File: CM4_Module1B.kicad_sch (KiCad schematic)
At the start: 10 parts, among them J18 179-UJ20CHC4SMTTR

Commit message: chore: Many routing changes
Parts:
- removed J18: 179-UJ20CHC4SMTTR, dz_con:CON_Samesky_CUI_UJ20-C-H-C-4-SMT-TR, symbol #dzdb:s_con/SAME-179-UJ20CHC4SMTTR
- added J3: 179-UJ20CHC4SMTTR, dz_con:CON_Samesky_CUI_UJ20-C-H-C-4-SMT-TR, symbol #dzdb:s_con/SAME-179-UJ20CHC4SMTTR
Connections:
- net GND: now also J3.A12_B1 (GND), J3.A1_B12 (GND)
- net USB_D+: now also J3.A6 (DP1), J3.B6 (DP2)
- net USB_D-: now also J3.A7 (DN1), J3.B7 (DN2)
- net at C20.2, R11.1: now also J3.SH1 (SHIELD), J3.SH2 (SHIELD), J3.SH3 (SHIELD), J3.SH4 (SHIELD)
- net at R10.1: now also J3.A5 (CC1)
- net at R12.1: now also J3.B5 (CC2)
- net PCIe_CLK_N renamed PCIE_CLK._N
- net PCIe_CLK_P renamed PCIE_CLK._P
- net PCIe_RX_N renamed PCIE_RX._N
- net PCIe_RX_P renamed PCIE_RX._P
- net PCIe_TX_N renamed PCIE_TX._N
- net PCIe_TX_P renamed PCIE_TX._P
- net USB_Out_5V renamed USB_OTG_5V
- net USB_OTG_5V: now also J3.A4_B9 (VBUS), J3.A9_B4 (VBUS)
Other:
- note removed: "indicator LED :)"
- note removed: "reduce EMI"
- moved on the sheet: C20, D5, D6, R10, R11, R12, R9

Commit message: chore: more cleanup
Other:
- company: (none) -> Davide
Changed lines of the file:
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@@
 	(generator_version "9.0")
 	(paper "A4")
+	(title_block
+		(date "2025-11-18")
+		(company "Davide")
+	)
 	(text "old usb port for reference."
 		(exclude_from_sim no)

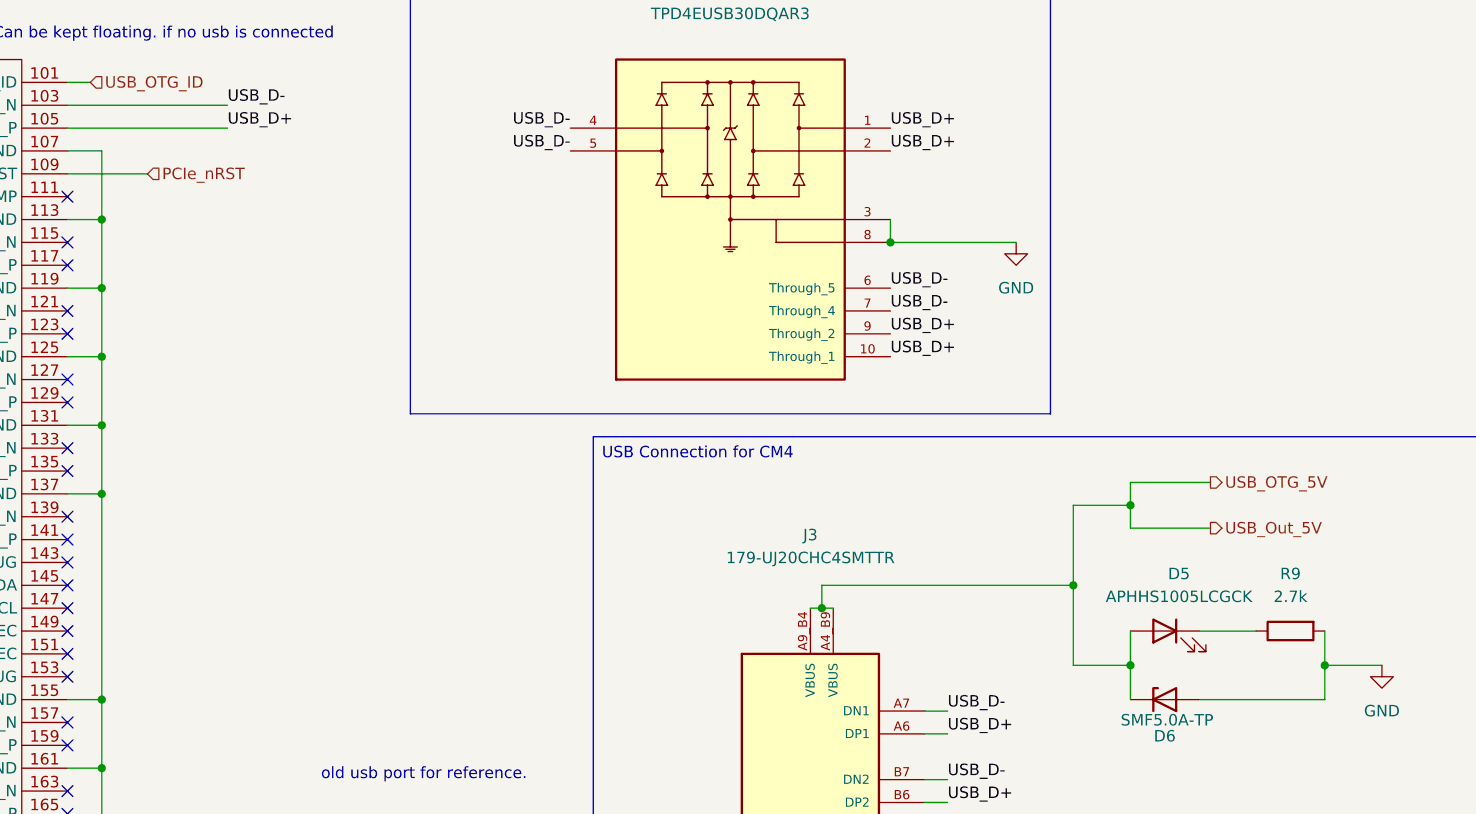
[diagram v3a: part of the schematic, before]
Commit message: chore: added LED indicators for power and activity status, updated symbold, rerouted some things for better visibility
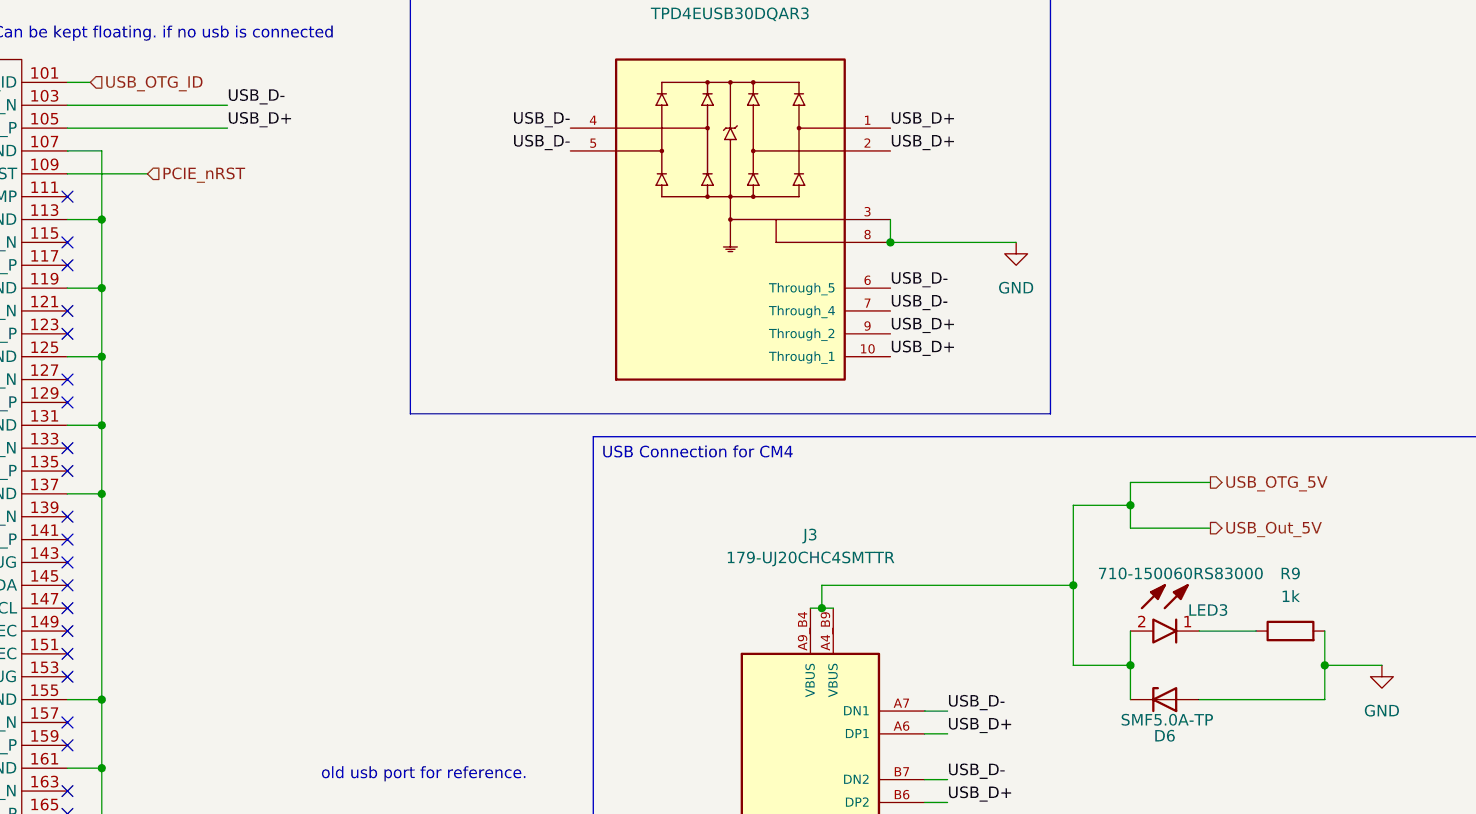
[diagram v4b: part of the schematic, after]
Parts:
- removed D5: APHHS1005LCGCK, LED_SMD:LED_0402_1005Metric, symbol #dzdb:s_dio/D-KIN-APHHS1005LCGCK
- removed R9: 2.7k, Resistor_SMD:R_0603_1608Metric, symbol #dzdb:g_res/R-2.7k-0603
- added LED3: 710-150060RS83000, dz_dio:Wuerth_LED_150060RS83000, symbol #dzdb:s_dio/D-WURT-710-150060RS83000
- added R9: 1k, Resistor_SMD:R_0603_1608Metric, symbol #dzdb:g_res/R-1k-0603
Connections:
- net GND: now also R9.2
- net USB_OTG_5V: now also LED3.2 (A)
- net PCIe_nRST renamed PCIE_nRST
- new net: LED3.1 (K), R9.1

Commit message: chore: Loads of redoing stuff. Added a Changelog
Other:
- title: (none) -> Nautilus_Mainboard
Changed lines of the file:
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@@
 	(paper "A4")
 	(title_block
+		(title "Nautilus_Mainboard")
 		(date "2025-11-19")
 		(rev "0")

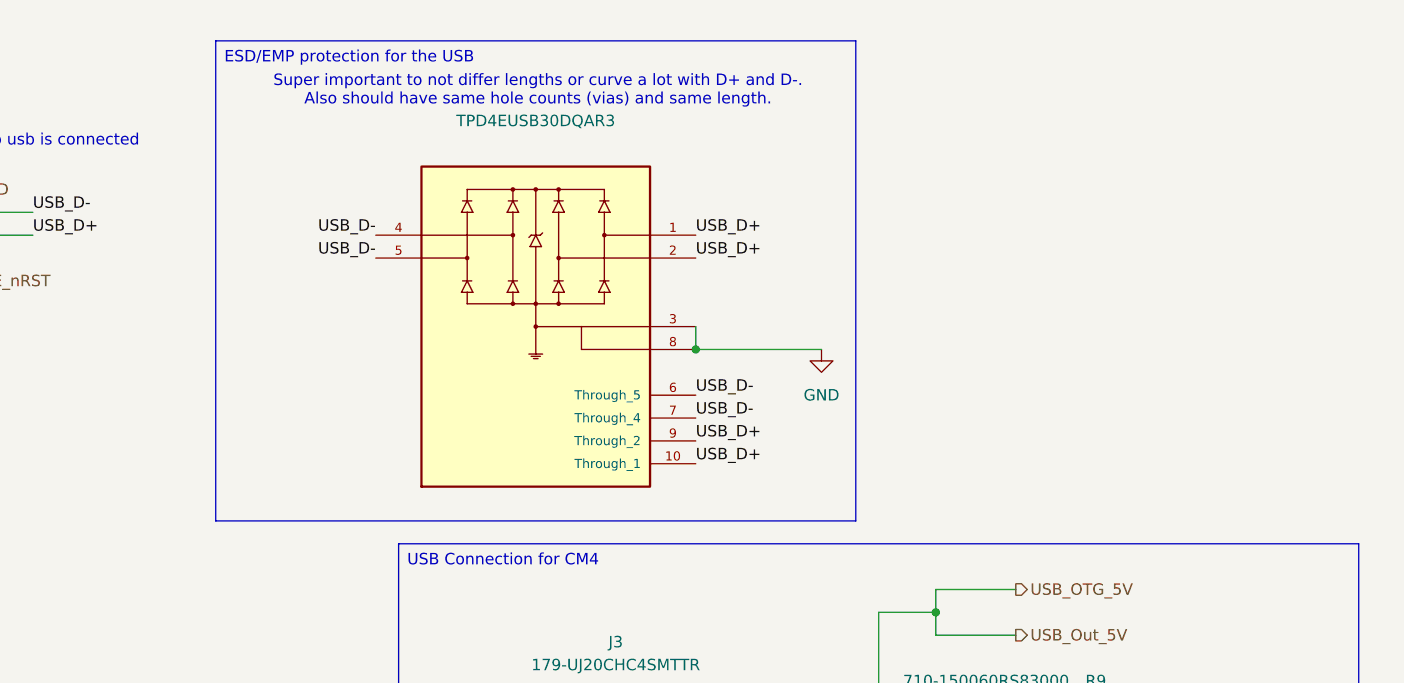
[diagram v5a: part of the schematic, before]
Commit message: chore: routed many parts together. added testpoints
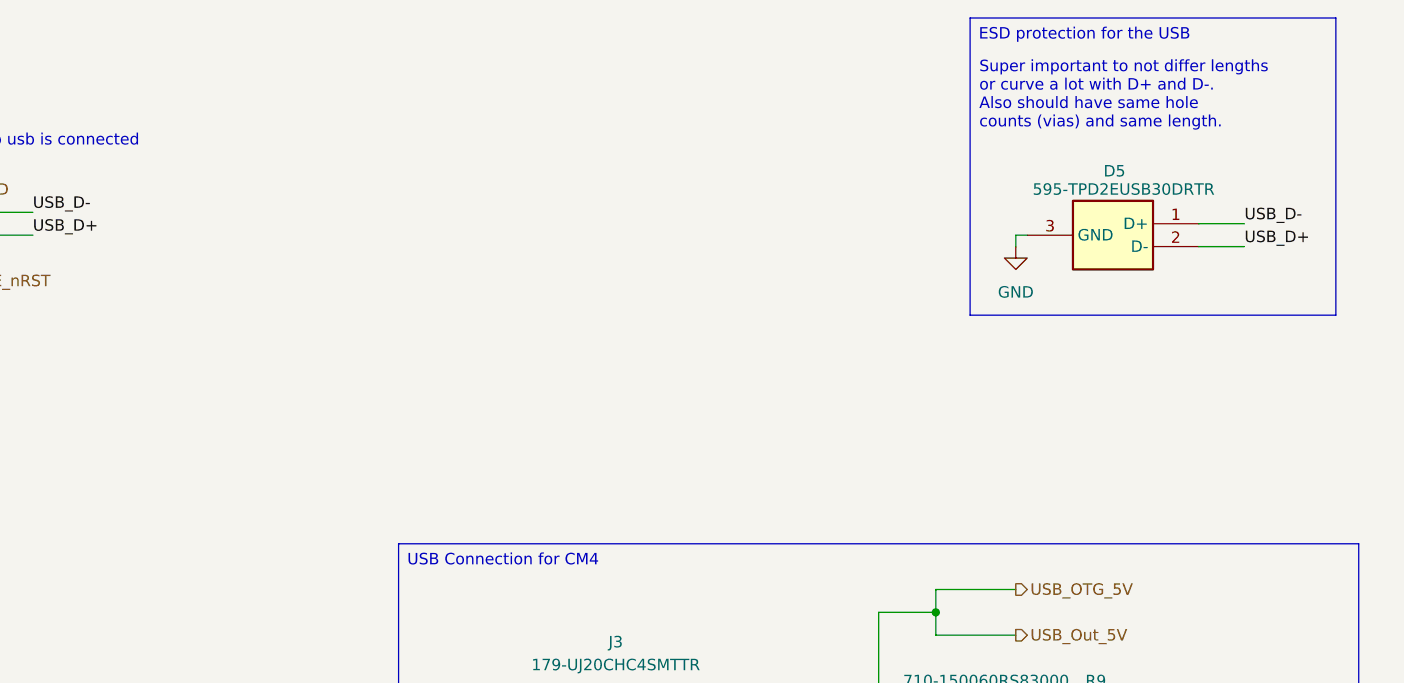
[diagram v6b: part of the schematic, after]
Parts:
- removed TPD4EUSB30DQAR3: ~, dz_con:IC_TPD4EUSB30DQAR, symbol #dzdb:s_misc/IC-ESD-TPD4EUSB30
- added D5: 595-TPD2EUSB30DRTR, dz_dio:TI_Prot_TPD2EUSB30DRTR, symbol #dzdb:s_dio/TEXA-595-TPD2EUSB30DRTR
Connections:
- net GND: now also D5.3 (GND)
- net USB_D+: now also D5.2 (D-)
- net USB_D-: now also D5.1 (D+)

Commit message: fix: minor changes, preparations for BOM and gerber, added Stitching
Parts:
- Module1: Comment (none) -> lifecycle=Active; note=100-pin 0.4mm pitch connector; LCSC lifecycle=Active; note=100-pin 0.4mm pitch connector -> N/A; Pin Count Mouser -> 51; SPN https://www.lcsc.com/datasheet/C597931.pdf -> 798-DF40C100DS0.4V51; Supplier N/A -> mouser
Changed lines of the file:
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@@
+			)
+		)
+		(property "Field16" ""
+			(at 241.3 102.87 0)
+			(effects
+				(font
+					(size 1.27 1.27)
+				)
+				(hide yes)
+			)
+		)
+		(property "Sim.Pins" ""
+			(at 241.3 102.87 0)
+			(effects
+				(font
+					(size 1.27 1.27)
+				)
+				(hide yes)
 			)
 		)
@@
 			)
 		)
+		(property "Field16" ""
+			(at 257.81 39.37 0)
+			(effects
+				(font
+					(size 1.27 1.27)
+				)
+				(hide yes)
+			)
+		)
+		(property "Sim.Pins" ""
+			(at 257.81 39.37 0)
+			(effects
+				(font
+					(size 1.27 1.27)
+				)
+				(hide yes)
+			)
+		)
 		(pin "2"
 		)
@@
 			)
 		)
+		(property "Field16" ""
+			(at 255.27 95.25 90)
+			(effects
+				(font
+					(size 1.27 1.27)
+				)
+				(hide yes)
+			)
+		)
+		(property "Sim.Pins" ""
+			(at 255.27 95.25 90)
+			(effects
+				(font
+					(size 1.27 1.27)
+				)
+				(hide yes)
+			)
+		)
 		(pin "1"
 		)
@@
 			)
 		)
+		(property "Field16" ""
+			(at 210.82 148.59 90)
+			(effects
+				(font
+					(size 1.27 1.27)
+				)
+				(hide yes)
+			)
+		)
+		(property "Sim.Pins" ""
+			(at 210.82 148.59 90)
+			(effects
+				(font
+					(size 1.27 1.27)
+				)
+				(hide yes)
+			)
+		)
 		(pin "2"
 		)
@@
 			)
 		)
-		(property "Datasheet" ""
+		(property "Datasheet" "https://www.lcsc.com/datasheet/C597931.pdf"
 			(at 91.44 121.92 0)
 			(effects
@@
 			)
 		)
-		(property "Pin Count" "Mouser"
+		(property "Pin Count" "51"
 			(at -50.8 95.25 0)
 			(effects
@@
 			)
 		)
-		(property "Supplier" "N/A"
+		(property "Supplier" "mouser"
 			(at -50.8 95.25 0)
 			(effects
@@
 			)
 		)
-		(property "SPN" "https://www.lcsc.com/datasheet/C597931.pdf"
+		(property "SPN" "798-DF40C100DS0.4V51"
 			(at -50.8 95.25 0)
 			(effects
@@
 			)
 		)
-		(property "LCSC" "lifecycle=Active; note=100-pin 0.4mm pitch connector"
+		(property "LCSC" "N/A"
 			(at -50.8 95.25 0)
 			(effects
@@
 			)
 		)
-		(property "Comment" ""
+		(property "Comment" "lifecycle=Active; note=100-pin 0.4mm pitch connector"
+			(at -50.8 95.25 0)
+			(effects
+				(font
+					(size 1.27 1.27)
+				)
+				(hide yes)
+			)
+		)
+		(property "Field16" ""
+			(at -50.8 95.25 0)
+			(effects
+				(font
+					(size 1.27 1.27)
+				)
+				(hide yes)
+			)
+		)
+		(property "Sim.Pins" ""
 			(at -50.8 95.25 0)
 			(effects
@@
 			)
 		)
+		(property "Field16" ""
+			(at 210.82 144.78 90)
+			(effects
+				(font
+					(size 1.27 1.27)
+				)
+				(hide yes)
+			)
+		)
+		(property "Sim.Pins" ""
+			(at 210.82 144.78 90)
+			(effects
+				(font
+					(size 1.27 1.27)
+				)
+				(hide yes)
+			)
+		)
 		(pin "1"
 		)
@@
 			)
 		)
+		(property "Field16" ""
+			(at 218.44 119.38 90)
+			(effects
+				(font
+					(size 1.27 1.27)
+				)
+				(hide yes)
+			)
+		)
+		(property "Sim.Pins" ""
+			(at 218.44 119.38 90)
+			(effects
+				(font
+					(size 1.27 1.27)
+				)
+				(hide yes)
+			)
+		)
 		(pin "2"
 		)
@@
 		)
 		(property "Comment" "lifecycle=New Product; note=Auto-generated part for Same Sky / CUI USB Type-C connector family"
+			(at 201.93 116.84 0)
+			(effects
+				(font
+					(size 1.27 1.27)
+				)
+				(hide yes)
+			)
+		)
+		(property "Field16" ""
+			(at 201.93 116.84 0)
+			(effects
+				(font
+					(size 1.27 1.27)
+				)
+				(hide yes)
+			)
+		)
+		(property "Sim.Pins" ""
 			(at 201.93 116.84 0)
 			(effects
@@
 			)
 		)
+		(property "Field16" ""
+			(at 241.3 95.25 0)
+			(effects
+				(font
+					(size 1.27 1.27)
+				)
+				(hide yes)
+			)
+		)
+		(property "Sim.Pins" ""
+			(at 241.3 95.25 0)
+			(effects
+				(font
+					(size 1.27 1.27)
+				)
+				(hide yes)
+			)
+		)
 		(pin "2"
 		)
@@
 			(effects
 				(font
+					(size 1.27 1.27)
+				)
+				(hide yes)
+			)
+		)
+		(property "Field16" ""
+			(at 218.44 127 90)
+			(effects
+				(font
+					(size 1.27 1.27)
+				)
+				(hide yes)
+			)
+		)
+		(property "Sim.Pins" ""
+			(at 218.44 127 90)
+			(effects
+				(font
